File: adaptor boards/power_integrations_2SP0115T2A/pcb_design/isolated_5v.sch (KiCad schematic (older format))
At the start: 10 parts, among them T1 TRANS-2CT, U2 SN6501DBV, U4 TPS76350

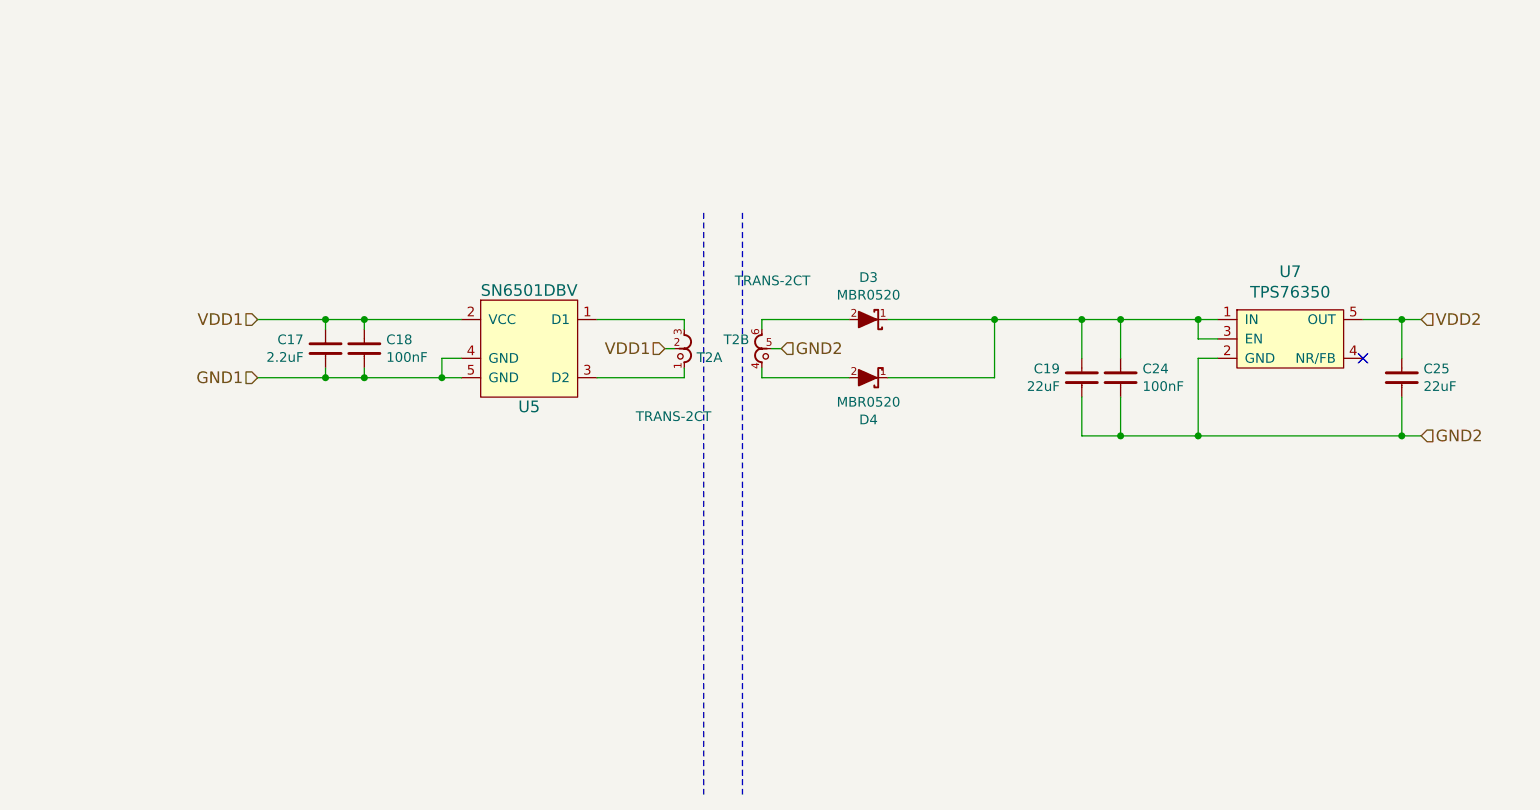
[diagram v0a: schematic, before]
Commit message: Fix swapped differential signals in the interface board
Signed-off-by: Marcos Chaparro <mchaparro@paltatech.com>
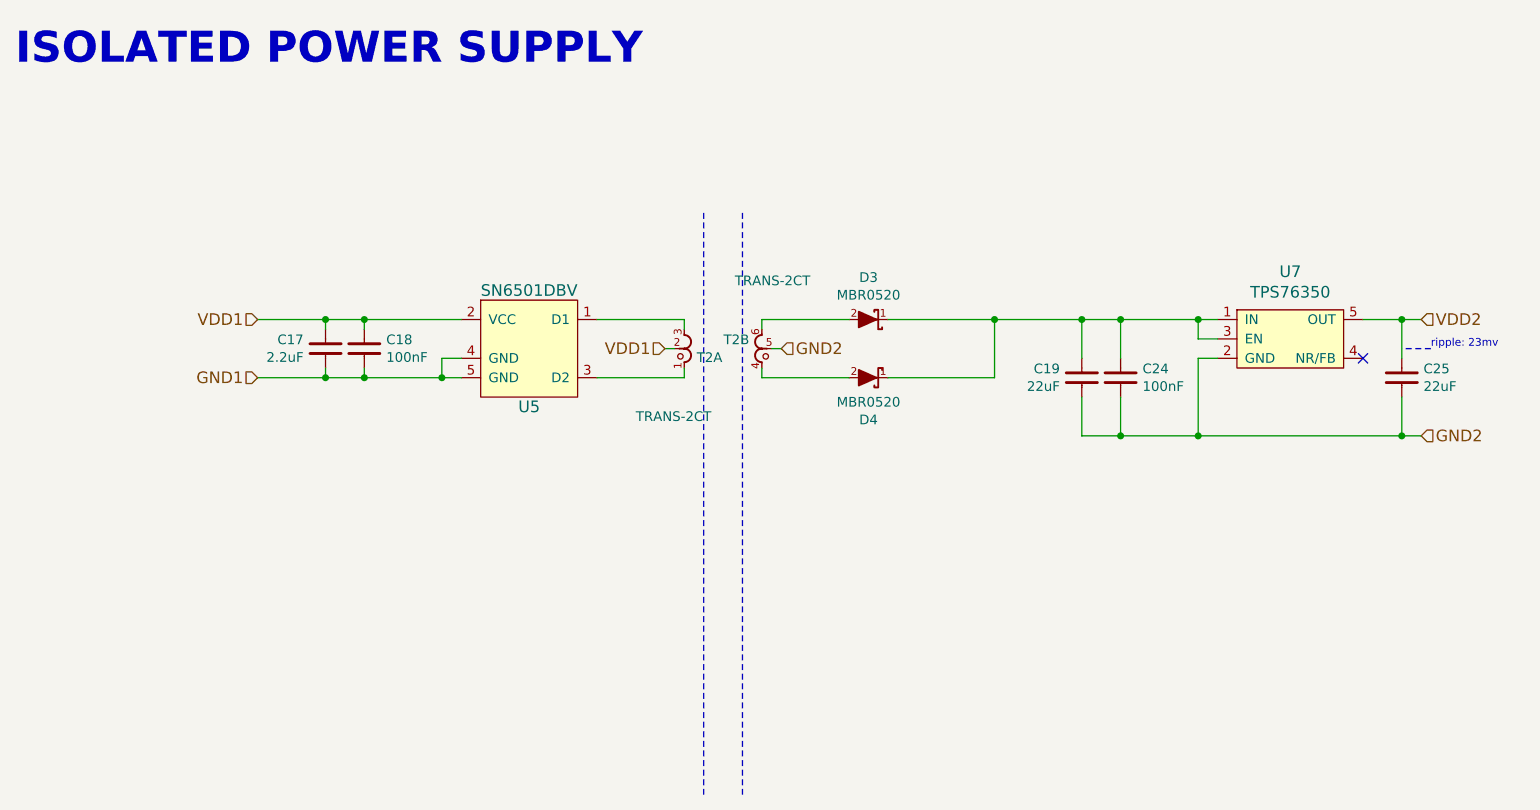
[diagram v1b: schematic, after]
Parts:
- C10, C16: MFR (none) -> TDK Corporation; MPN (none) -> C2012X5R1V226M125AC; SPN (none) -> 445-14428-1-ND; SPR (none) -> Digikey
- C15, C9: MFR (none) -> Murata Electronics North America; MPN (none) -> GRM188R71E104KA01D; SPN (none) -> 490-1524-1-ND; SPR (none) -> Digikey
- C8: MFR (none) -> Murata Electronics North America; MPN (none) -> GRM188R71A225KE15D; SPN (none) -> 490-4520-1-ND; SPR (none) -> Digikey
- D1, D2: MFR (none) -> ON Semiconductor; MPN (none) -> MBR0520LT1G; SPN (none) -> MBR0520LT1GOSCT-ND; SPR (none) -> Digikey
- T1: MFR (none) -> Wurth Electronics Midcom; MPN (none) -> 760390014; SPN (none) -> 732-4458-1-ND; SPR (none) -> Digikey
- U2: MFR (none) -> Texas Instruments; MPN (none) -> SN6501DBVR; SPN (none) -> 296-37700-1-ND; SPR (none) -> Digikey
- U4: MFR (none) -> Texas Instruments; MPN (none) -> TPS76350DBVR; SPN (none) -> 296-11023-1-ND; SPR (none) -> Digikey
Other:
- note added: "ISOLATED POWER SUPPLY"
- note added: "ripple: 23mv"
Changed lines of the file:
@@
-EESchema Schematic File Version 2
+EESchema Schematic File Version 3
 LIBS:Abracon
 LIBS:ActiveSemi
@@
 Comment4 ""
 $EndDescr
-Wire Notes Line
-	5100 2350 5100 5350
-Wire Notes Line
-	4900 2350 4900 5350
 $Comp
 L SN6501DBV U2
@@
 F 1 "SN6501DBV" H 4000 3350 60  0000 C CNN
 F 2 "smd-semi:SOT-23-5" H -2350 750 60  0001 C CNN
-F 3 "" H -2350 750 60  0001 C CNN
+F 3 "http://www.ti.com/lit/ds/symlink/sn6501.pdf" H -2350 750 60  0001 C CNN
+F 4 "Texas Instruments" H 0   0   50  0001 C CNN "MFR"
+F 5 "SN6501DBVR" H 0   0   50  0001 C CNN "MPN"
+F 6 "Digikey" H 0   0   50  0001 C CNN "SPR"
+F 7 "296-37700-1-ND" H 0   0   50  0001 C CNN "SPN"
+F 8 "" H 0   0   50  0001 C CNN "SPURL"
 	1    4000 3050
 	1    0    0    -1
 $EndComp
-Wire Wire Line
-	3650 3200 2600 3200
-Wire Wire Line
-	3550 3200 3550 3100
-Wire Wire Line
-	3550 3100 3650 3100
-Text HLabel 2600 2900 0    60   Input ~ 0
-VDD1
 $Comp
 L C-1206 C?
@@
 F 1 "2.2uF" H 3063 3005 50  0000 L CNN
 F 2 "IPC7351-Nominal:CAPC1608X55" H 2950 3050 50  0001 C CNN
-F 3 "" H 2940 3025 60  0000 C CNN
+F 3 "" H 2940 3025 60  0001 C CNN
 F 4 "CAP MLCC 100pF C0G 50V 5% [0603]" H 3750 3600 60  0001 C CNN "BOM"
+F 5 "Murata Electronics North America" H 0   0   50  0001 C CNN "MFR"
+F 6 "GRM188R71A225KE15D" H 0   0   50  0001 C CNN "MPN"
+F 7 "Digikey" H 0   0   50  0001 C CNN "SPR"
+F 8 "490-4520-1-ND" H 0   0   50  0001 C CNN "SPN"
+F 9 "" H 0   0   50  0001 C CNN "SPURL"
 	1    2950 3050
 	-1   0    0    -1
@@
 F 1 "100nF" H 3263 3005 50  0000 L CNN
 F 2 "IPC7351-Nominal:CAPC1608X55" H 3150 3050 50  0001 C CNN
-F 3 "" H 3140 3025 60  0000 C CNN
+F 3 "" H 3140 3025 60  0001 C CNN
 F 4 "CAP MLCC 100pF C0G 50V 5% [0603]" H 3950 3600 60  0001 C CNN "BOM"
+F 5 "Murata Electronics North America" H 0   0   50  0001 C CNN "MFR"
+F 6 "GRM188R71E104KA01D" H 0   0   50  0001 C CNN "MPN"
+F 7 "Digikey" H 0   0   50  0001 C CNN "SPR"
+F 8 "490-1524-1-ND" H 0   0   50  0001 C CNN "SPN"
+F 9 "" H 0   0   50  0001 C CNN "SPURL"
 	1    3150 3050
 	1    0    0    -1
 $EndComp
-Wire Wire Line
-	3650 2900 2600 2900
-Connection ~ 3150 2900
-Text HLabel 2600 3200 0    60   Input ~ 0
-GND1
-Connection ~ 2950 2900
-Text HLabel 4700 3050 0    60   Input ~ 0
-VDD1
-Text HLabel 5300 3050 2    60   Input ~ 0
-GND2
 $Comp
 L MBR0520 D1
@@
 F 4 "MBR0520LT1G" H 5750 2900 60  0001 C CNN "mfg#"
 F 5 "SCHOTTKY MBR0520LT1G" H 1200 250 60  0001 C CNN "BOM"
+F 6 "ON Semiconductor" H 0   0   50  0001 C CNN "MFR"
+F 7 "MBR0520LT1G" H 0   0   50  0001 C CNN "MPN"
+F 8 "Digikey" H 0   0   50  0001 C CNN "SPR"
+F 9 "MBR0520LT1GOSCT-ND" H 0   0   50  0001 C CNN "SPN"
+F 10 "" H 0   0   50  0001 C CNN "SPURL"
 	1    5750 2900
 	0    -1   1    0
@@
 F 4 "MBR0520LT1G" H 5750 3200 60  0001 C CNN "mfg#"
 F 5 "SCHOTTKY MBR0520MBR0520LT1G" H 1200 550 60  0001 C CNN "BOM"
+F 6 "ON Semiconductor" H 0   0   50  0001 C CNN "MFR"
+F 7 "MBR0520LT1G" H 0   0   50  0001 C CNN "MPN"
+F 8 "Digikey" H 0   0   50  0001 C CNN "SPR"
+F 9 "MBR0520LT1GOSCT-ND" H 0   0   50  0001 C CNN "SPN"
+F 10 "" H 0   0   50  0001 C CNN "SPURL"
 	1    5750 3200
 	0    -1   -1   0
 $EndComp
-Wire Wire Line
-	5650 2900 5200 2900
-Wire Wire Line
-	5200 2900 5200 2950
-Wire Wire Line
-	5850 3200 6400 3200
-Wire Wire Line
-	6400 3200 6400 2900
-Wire Wire Line
-	7550 2900 5850 2900
-Connection ~ 6400 2900
 $Comp
 L C-0805 C?
@@
 F 1 "22uF" H 6963 3155 50  0000 L CNN
 F 2 "IPC7351-Nominal:CAPC2012X70" H 3250 1000 50  0001 C CNN
-F 3 "" H 3240 975 60  0000 C CNN
+F 3 "" H 3240 975 60  0001 C CNN
 F 4 "CAP MLCC 100pF C0G 50V 5% [0805]" H 4050 1550 60  0001 C CNN "BOM"
+F 5 "TDK Corporation" H 0   0   50  0001 C CNN "MFR"
+F 6 "C2012X5R1V226M125AC" H 0   0   50  0001 C CNN "MPN"
+F 7 "Digikey" H 0   0   50  0001 C CNN "SPR"
+F 8 "445-14428-1-ND" H 0   0   50  0001 C CNN "SPN"
+F 9 "" H 0   0   50  0001 C CNN "SPURL"
 	1    6850 3200
 	-1   0    0    -1
 $EndComp
-Wire Wire Line
-	6850 3100 6850 2900
 $Comp
 L C-1206 C?
@@
 F 1 "100nF" H 7163 3155 50  0000 L CNN
 F 2 "IPC7351-Nominal:CAPC1608X55" H 7050 3200 50  0001 C CNN
-F 3 "" H 7040 3175 60  0000 C CNN
+F 3 "" H 7040 3175 60  0001 C CNN
 F 4 "CAP MLCC 100pF C0G 50V 5% [0603]" H 7850 3750 60  0001 C CNN "BOM"
+F 5 "Murata Electronics North America" H 0   0   50  0001 C CNN "MFR"
+F 6 "GRM188R71E104KA01D" H 0   0   50  0001 C CNN "MPN"
+F 7 "Digikey" H 0   0   50  0001 C CNN "SPR"
+F 8 "490-1524-1-ND" H 0   0   50  0001 C CNN "SPN"
+F 9 "" H 0   0   50  0001 C CNN "SPURL"
 	1    7050 3200
 	1    0    0    -1
 $EndComp
-Wire Wire Line
-	7050 3100 7050 2900
-Connection ~ 6850 2900
 $Comp
 L TPS76350 U4
@@
 F 1 "TPS76350" H 7925 3241 60  0000 C CNN
 F 2 "smd-semi:SOT-23-5" H 7950 2750 60  0001 C CNN
-F 3 "" H 4900 400 60  0000 C CNN
+F 3 "http://www.ti.com/lit/ds/symlink/tps763.pdf" H 4900 400 60  0001 C CNN
+F 4 "Texas Instruments" H 0   0   50  0001 C CNN "MFR"
+F 5 "TPS76350DBVR" H 0   0   50  0001 C CNN "MPN"
+F 6 "Digikey" H 0   0   50  0001 C CNN "SPR"
+F 7 "296-11023-1-ND" H 0   0   50  0001 C CNN "SPN"
+F 8 "" H 0   0   50  0001 C CNN "SPURL"
 	1    7950 3000
 	1    0    0    -1
 $EndComp
-Connection ~ 7050 2900
-Wire Wire Line
-	7550 3000 7450 3000
-Wire Wire Line
-	7450 3000 7450 2900
-Connection ~ 7450 2900
-Wire Wire Line
-	7550 3100 7450 3100
-Wire Wire Line
-	7450 3100 7450 3500
-Wire Wire Line
-	8600 3500 6850 3500
-Wire Wire Line
-	6850 3500 6850 3300
-Wire Wire Line
-	7050 3500 7050 3300
-Connection ~ 7050 3500
 $Comp
 L C-0805 C?
@@
 F 1 "22uF" H 8612 3155 50  0000 L CNN
 F 2 "IPC7351-Nominal:CAPC2012X70" H 4900 1000 50  0001 C CNN
-F 3 "" H 4890 975 60  0000 C CNN
+F 3 "" H 4890 975 60  0001 C CNN
 F 4 "CAP MLCC 100pF C0G 50V 5% [0805]" H 5700 1550 60  0001 C CNN "BOM"
+F 5 "TDK Corporation" H 0   0   50  0001 C CNN "MFR"
+F 6 "C2012X5R1V226M125AC" H 0   0   50  0001 C CNN "MPN"
+F 7 "Digikey" H 0   0   50  0001 C CNN "SPR"
+F 8 "445-14428-1-ND" H 0   0   50  0001 C CNN "SPN"
+F 9 "" H 0   0   50  0001 C CNN "SPURL"
 	1    8500 3200
 	1    0    0    -1
 $EndComp
-NoConn ~ 8300 3100
-Wire Wire Line
-	8500 3100 8500 2900
-Wire Wire Line
-	8600 2900 8300 2900
-Wire Wire Line
-	8500 3300 8500 3500
-Connection ~ 7450 3500
-Text HLabel 8600 2900 2    60   Input ~ 0
-VDD2
-Connection ~ 8500 2900
-Text HLabel 8600 3500 2    60   Input ~ 0
-GND2
-Connection ~ 8500 3500
 $Comp
 L TRANS-2CT T?
@@
 F 1 "TRANS-2CT" H 5050 3400 50  0000 R CNN
 F 2 "manuf:WURTH-760390014" H 4650 2800 60  0001 C CNN
-F 3 "" H -1000 850 60  0000 C CNN
+F 3 "http://katalog.we-online.de/ctm/datasheet/760390014.pdf" H -1000 850 60  0001 C CNN
+F 4 "Wurth Electronics Midcom" H 0   0   50  0001 C CNN "MFR"
+F 5 "760390014" H 0   0   50  0001 C CNN "MPN"
+F 6 "Digikey" H 0   0   50  0001 C CNN "SPR"
+F 7 "732-4458-1-ND" H 0   0   50  0001 C CNN "SPN"
+F 8 "" H 0   0   50  0001 C CNN "SPURL"
 	1    4800 3050
 	-1   0    0    1
 $EndComp
-Wire Wire Line
-	4700 3050 4750 3050
 $Comp
 L TRANS-2CT T?
@@
 F 1 "TRANS-2CT" H 5450 2700 50  0000 R CNN
 F 2 "manuf:WURTH-760390014" H 5100 3400 60  0001 C CNN
-F 3 "" H -450 850 60  0000 C CNN
+F 3 "http://katalog.we-online.de/ctm/datasheet/760390014.pdf" H -450 850 60  0001 C CNN
+F 4 "Wurth Electronics Midcom" H 0   0   50  0001 C CNN "MFR"
+F 5 "760390014" H 0   0   50  0001 C CNN "MPN"
+F 6 "Digikey" H 0   0   50  0001 C CNN "SPR"
+F 7 "732-4458-1-ND" H 0   0   50  0001 C CNN "SPN"
+F 8 "" H 0   0   50  0001 C CNN "SPURL"
 	2    5200 3050
 	1    0    0    1
 $EndComp
+Text HLabel 2600 2900 0    60   Input ~ 0
+VDD1
+Text HLabel 2600 3200 0    60   Input ~ 0
+GND1
+Text HLabel 4700 3050 0    60   Input ~ 0
+VDD1
+Text HLabel 5300 3050 2    60   Input ~ 0
+GND2
+Text HLabel 8600 2900 2    60   Input ~ 0
+VDD2
+Text HLabel 8600 3500 2    60   Input ~ 0
+GND2
+Wire Notes Line
+	5100 2350 5100 5350
+Wire Notes Line
+	4900 2350 4900 5350
+Wire Wire Line
+	3650 3200 2600 3200
+Wire Wire Line
+	3550 3200 3550 3100
+Wire Wire Line
+	3550 3100 3650 3100
+Wire Wire Line
+	3650 2900 2600 2900
+Wire Wire Line
+	5650 2900 5200 2900
+Wire Wire Line
+	5200 2900 5200 2950
+Wire Wire Line
+	5850 3200 6400 3200
+Wire Wire Line
+	6400 3200 6400 2900
+Wire Wire Line
+	7550 2900 5850 2900
+Wire Wire Line
+	6850 3100 6850 2900
+Wire Wire Line
+	7050 3100 7050 2900
+Wire Wire Line
+	7550 3000 7450 3000
+Wire Wire Line
+	7450 3000 7450 2900
+Wire Wire Line
+	7550 3100 7450 3100
+Wire Wire Line
+	7450 3100 7450 3500
+Wire Wire Line
+	8600 3500 6850 3500
+Wire Wire Line
+	6850 3500 6850 3300
+Wire Wire Line
+	7050 3500 7050 3300
+Wire Wire Line
+	8500 3100 8500 2900
+Wire Wire Line
+	8600 2900 8300 2900
+Wire Wire Line
+	8500 3300 8500 3500
+Wire Wire Line
+	4700 3050 4750 3050
 Wire Wire Line
 	5250 3050 5300 3050
@@
 Wire Wire Line
 	3150 3200 3150 3150
+Wire Wire Line
+	2950 3150 2950 3200
+Connection ~ 3150 2900
+Connection ~ 2950 2900
+Connection ~ 6400 2900
+Connection ~ 6850 2900
+Connection ~ 7050 2900
+Connection ~ 7450 2900
+Connection ~ 7050 3500
+Connection ~ 7450 3500
+Connection ~ 8500 2900
+Connection ~ 8500 3500
 Connection ~ 3550 3200
 Connection ~ 3150 3200
-Wire Wire Line
-	2950 3150 2950 3200
 Connection ~ 2950 3200
+NoConn ~ 8300 3100
+Text Notes 8650 3050 0    40   ~ 0
+ripple: 23mv
+Wire Notes Line
+	8650 3050 8500 3050
+Text Notes 1350 1600 0    160  ~ 32
+ISOLATED POWER SUPPLY
 $EndSCHEMATC
